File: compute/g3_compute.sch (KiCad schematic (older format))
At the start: 35 parts, among them J101 CONSMA001-SMD-G, J102 Temp_Connector_1x4, U101 PA1616D, U102 LoRa-E5

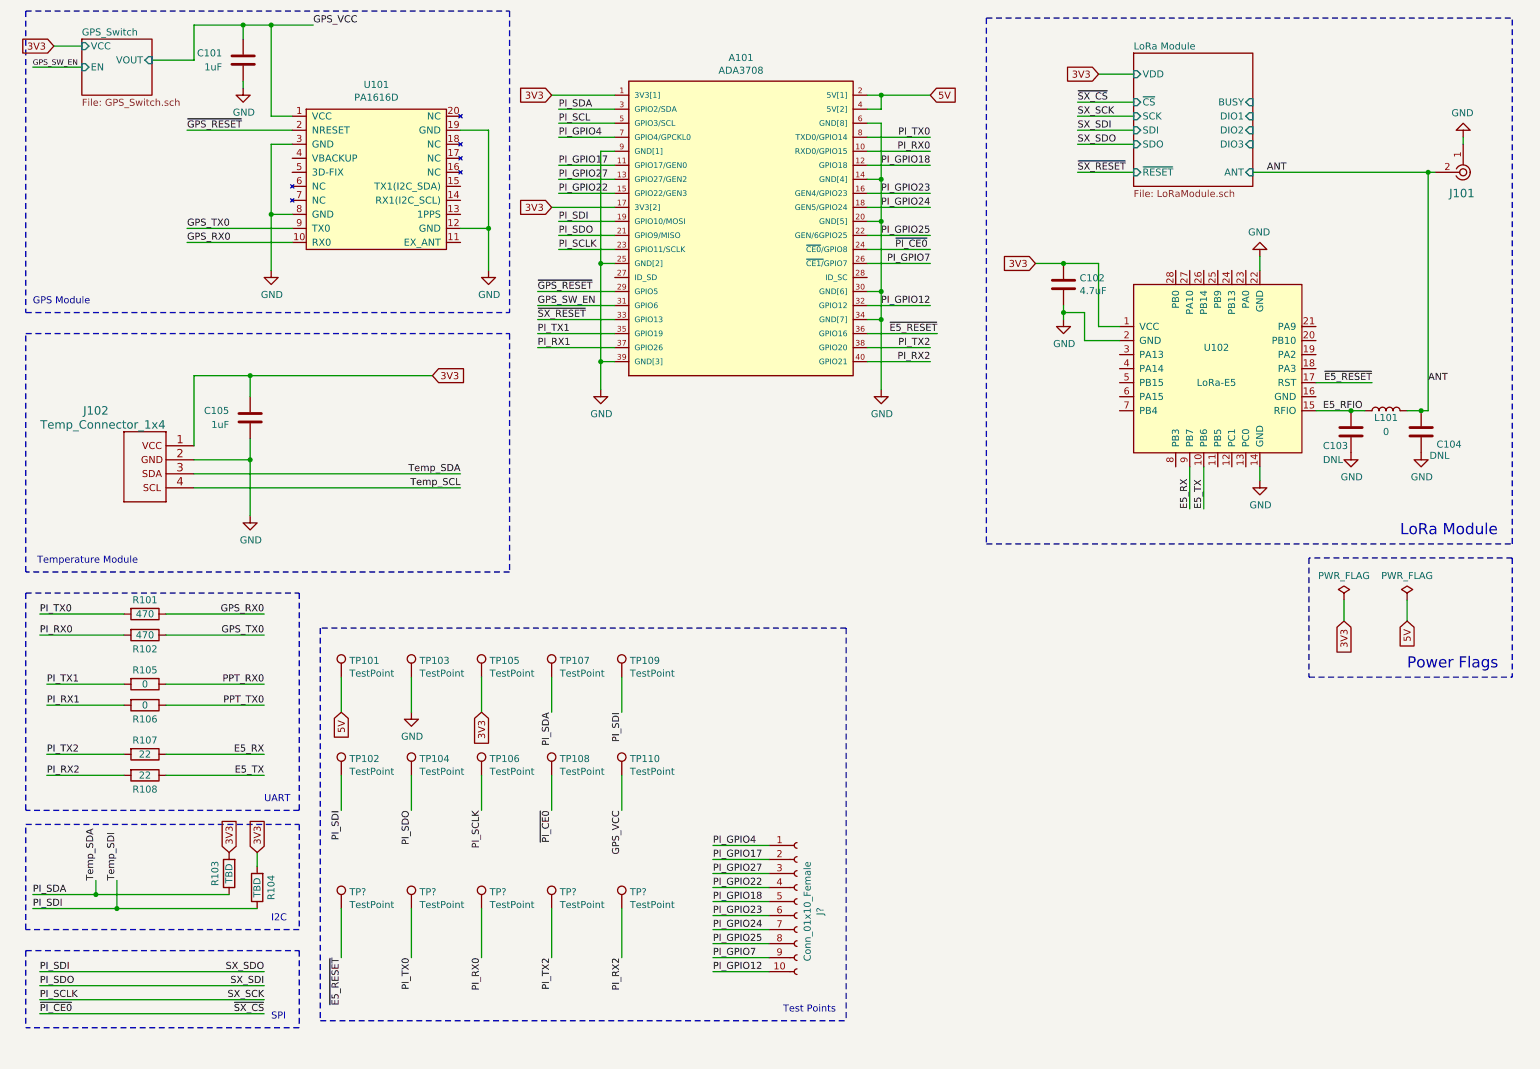
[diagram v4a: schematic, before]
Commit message: Adding Power Subsystem connector
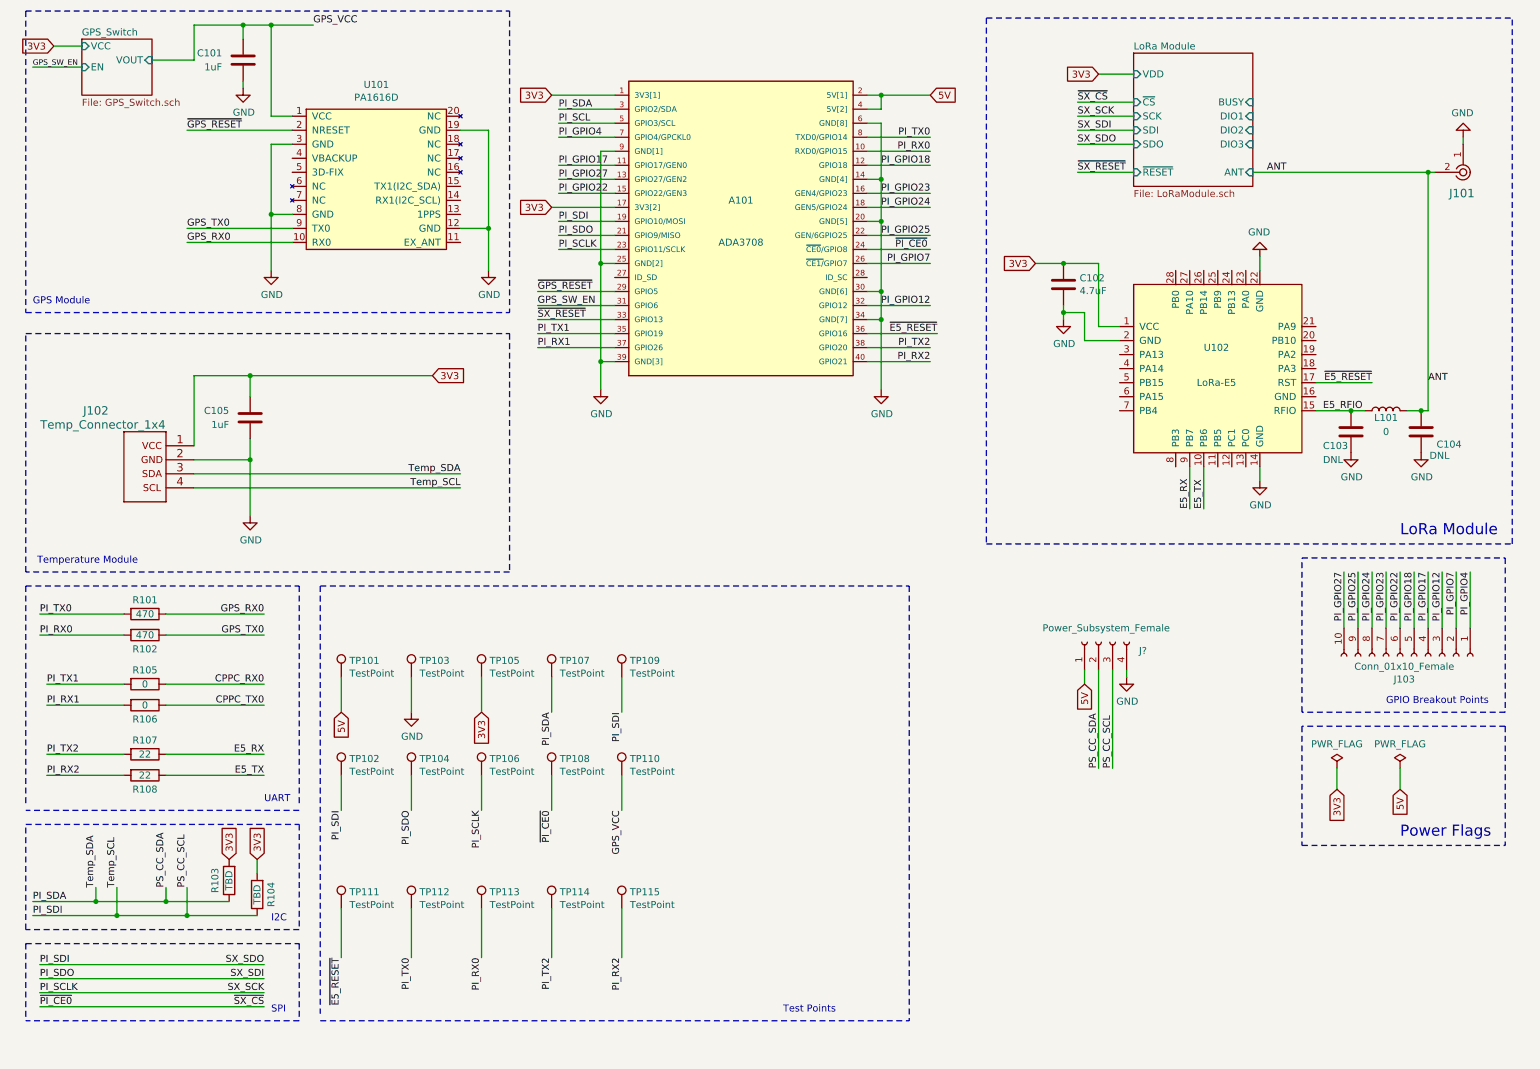
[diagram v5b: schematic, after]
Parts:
- added J?: Power_Subsystem_Female, Connector_Samtec_HLE_SMD:Samtec_HLE-102-02-xxx-DV_2x02_P2.54mm_Horizontal, symbol Connector:Conn_01x04_Female
- A101: Description Raspberry Pi Zero v1.3 -> (none); Notes (none) -> Raspberry Pi Zero v1.3
- gave numbers to parts that had none: 6
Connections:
- net Temp_SCL is gone; now on net PI_SDI: J102.4 (SCL)
- net 5V: now also J?.1 (Pin_1)
- net GND: now also J?.4 (Pin_4)
- net PI_GPIO12: now also J103.3 (Pin_3); no longer J103.10 (Pin_10)
- net PI_GPIO17: now also J103.4 (Pin_4); no longer J103.2 (Pin_2)
- net PI_GPIO22: now also J103.6 (Pin_6); no longer J103.4 (Pin_4)
- net PI_GPIO23: now also J103.7 (Pin_7); no longer J103.6 (Pin_6)
- net PI_GPIO24: now also J103.8 (Pin_8); no longer J103.7 (Pin_7)
- net PI_GPIO25: now also J103.9 (Pin_9); no longer J103.8 (Pin_8)
- net PI_GPIO27: now also J103.10 (Pin_10); no longer J103.3 (Pin_3)
- net PI_GPIO7: now also J103.2 (Pin_2); no longer J103.9 (Pin_9)
- net PI_SDA: now also J?.2 (Pin_2)
- net PI_SDI: now also J?.3 (Pin_3)
- net PPT_RX0 renamed CPPC_RX0
- net PPT_TX0 renamed CPPC_TX0
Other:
- note added: "GPIO Breakout Points"
- moved on the sheet: J103, R103, R104

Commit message: test points, footprints fixes, and layout fixes
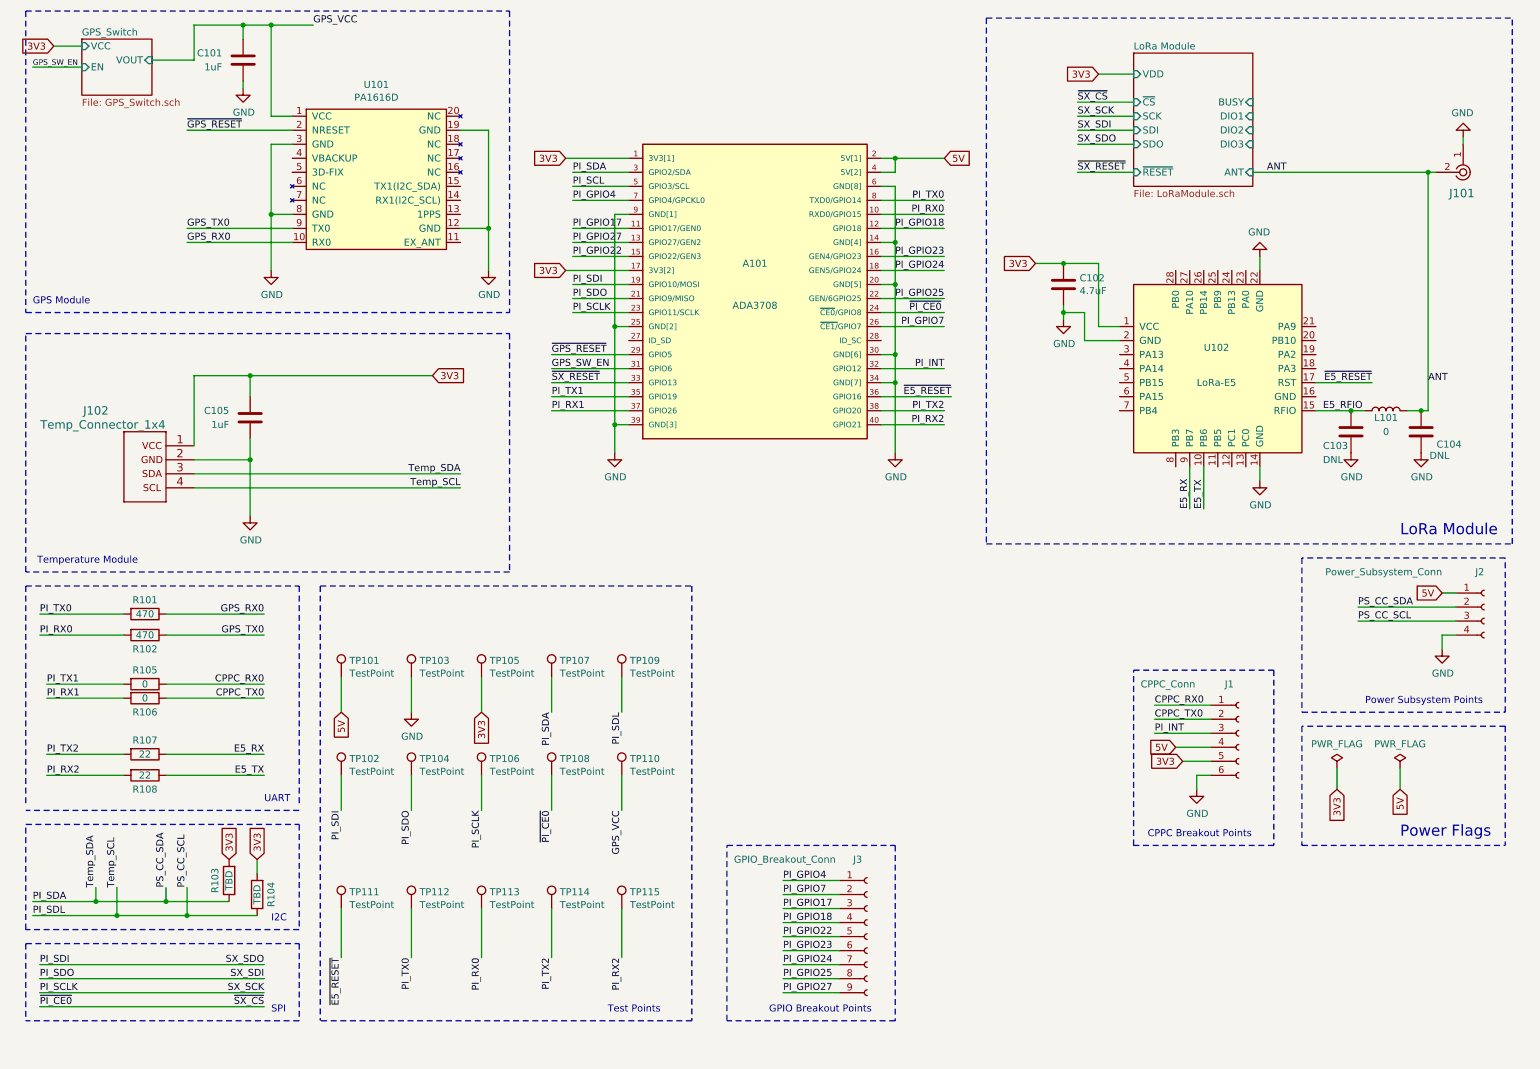
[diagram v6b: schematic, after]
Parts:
- removed J103: Conn_01x10_Female, symbol Connector:Conn_01x10_Female
- added J1: CPPC_Conn, Connector_Samtec_HLE_SMD:Samtec_HLE-103-02-xxx-DV_2x03_P2.54mm_Horizontal, symbol Connector:Conn_01x06_Female
- added J3: GPIO_Breakout_Conn, Connector_Samtec_HLE_SMD:Samtec_HLE-105-02-xxx-DV_2x05_P2.54mm_Horizontal, symbol Connector:Conn_01x09_Female
- A101: footprint ADA3708_RPI-ZERO -> Perch:ADA3708_RaspPiZero
- J2: renamed from J?; value Power_Subsystem_Female -> Power_Subsystem_Conn
- TP101, TP102, TP103, TP104, TP105, TP106, TP107, TP108, TP109, TP110, TP111, TP112, TP113, TP114, TP115: footprint (none) -> Capacitor_SMD:C_0805_2012Metric_Pad1.18x1.45mm_HandSolder
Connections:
- net 3V3: now also J1.5 (Pin_5)
- net 5V: now also J1.4 (Pin_4)
- net CPPC_RX0: now also J1.1 (Pin_1)
- net CPPC_TX0: now also J1.2 (Pin_2)
- net GND: now also J1.6 (Pin_6)
- net PI_GPIO17: now also J3.3 (Pin_3)
- net PI_GPIO18: now also J3.4 (Pin_4)
- net PI_GPIO22: now also J3.5 (Pin_5)
- net PI_GPIO23: now also J3.6 (Pin_6)
- net PI_GPIO24: now also J3.7 (Pin_7)
- net PI_GPIO25: now also J3.8 (Pin_8)
- net PI_GPIO27: now also J3.9 (Pin_9)
- net PI_GPIO4: now also J3.1 (Pin_1)
- net PI_GPIO7: now also J3.2 (Pin_2)
- net PI_SDI: no longer J102.4 (SCL), J2.3 (Pin_3), R104.1, TP109.1
- net PI_GPIO12 renamed PI_INT
- net PI_INT: now also J1.3 (Pin_3)
- new net PI_SDL: J102.4 (SCL), J2.3 (Pin_3), R104.1, TP109.1
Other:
- note added: "CPPC Breakout Points"
- note added: "Power Subsystem Points"
- moved on the sheet: A101, J2, R106

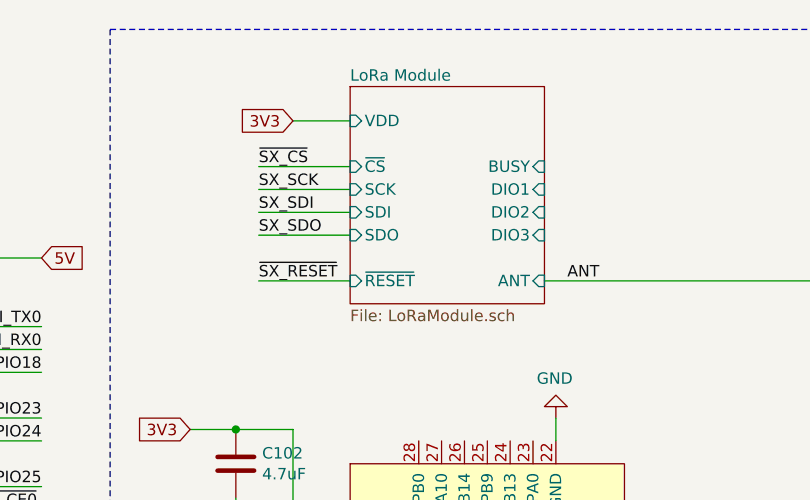
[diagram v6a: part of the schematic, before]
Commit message: Finishing Charge Controller Implementation
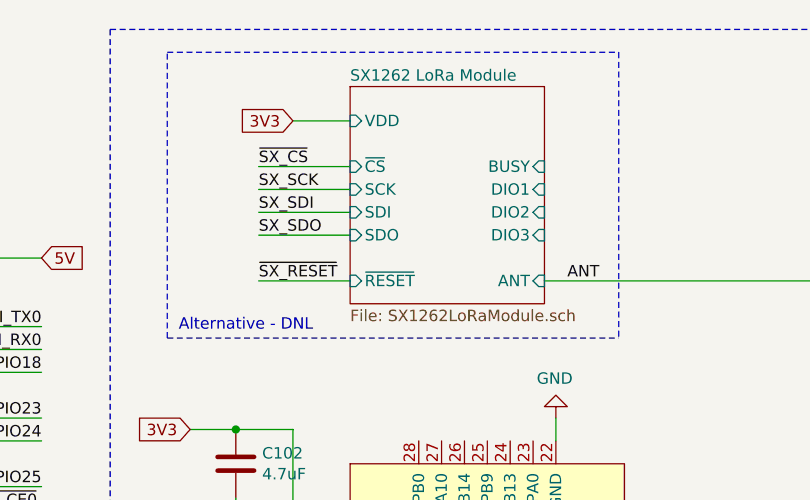
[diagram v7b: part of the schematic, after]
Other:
- note added: "Alternative - DNL"
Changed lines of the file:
@@
 encoding utf-8
 Sheet 1 3
-Title "G3 Compute System"
+Title "G3 Compute Subsystem"
 Date ""
 Rev "1"
@@
 S 8450 800  850  950
 U 618967E8
-F0 "LoRa Module" 50
-F1 "LoRaModule.sch" 50
+F0 "SX1262 LoRa Module" 50
+F1 "SX1262LoRaModule.sch" 50
 F2 "VDD" I L 8450 950 50
 F3 "~CS" I L 8450 1150 50
@@
 Wire Notes Line
 	8450 6450 8450 5200
+Wire Notes Line
+	9625 650  9625 1900
+Wire Notes Line
+	7650 1900 7650 650
+Text Notes 7700 1875 0    50   ~ 0
+Alternative - DNL
+Wire Notes Line
+	7650 1900 9625 1900
+Wire Notes Line
+	7650 650  9625 650
 $EndSCHEMATC
